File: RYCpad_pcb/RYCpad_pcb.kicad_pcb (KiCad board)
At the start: 2 copper layers, 77.2 x 117.6 mm, 66 parts, among them J1 USB_C_Receptacle_USB2.0, J2 AVR ISP, K1 KEYSW, K10 KEYSW, K11 KEYSW, K12 KEYSW, K13 KEYSW, K14 KEYSW, K15 KEYSW, K16 KEYSW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

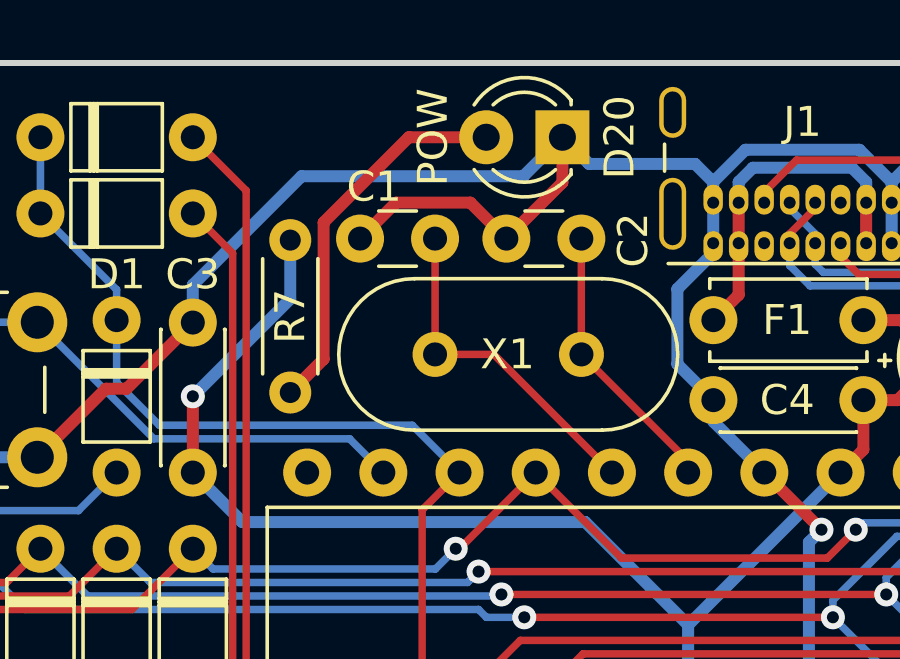
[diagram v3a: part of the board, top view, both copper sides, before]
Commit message: Make LED software-controlled
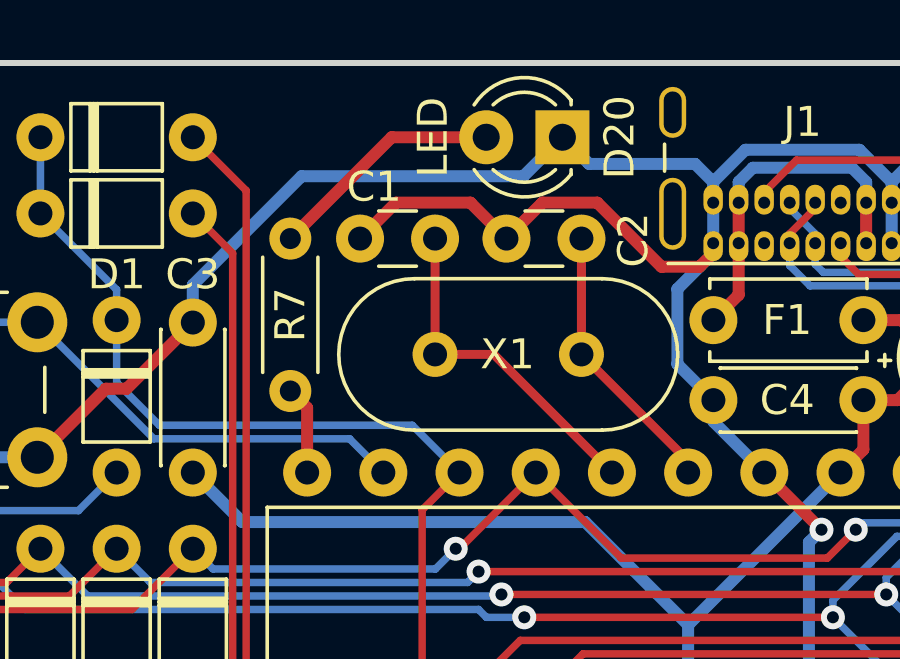
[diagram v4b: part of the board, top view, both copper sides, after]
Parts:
- C1, C2: value 22 -> 22p
- D20: value POW -> LED
- R5, R6: value 75 -> 68
- moved R7 5.13 mm to (-17.1, -54.2), turned to -90 degrees
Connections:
- J1 pad A8: Net-(J1-PadA8) -> unconnected-(J1-PadA8)
- J1 pad B8: Net-(J1-PadB8) -> unconnected-(J1-PadB8)
- J1 pad S1: Net-(J1-PadS1) -> unconnected-(J1-PadS1)
- R7 pad 2: +5V -> Net-(U1-Pad14)
- U1 pad 2: Net-(U1-Pad2) -> unconnected-(U1-Pad2)
- U1 pad 21: Net-(U1-Pad21) -> unconnected-(U1-Pad21)
- U1 pad 26: Net-(U1-Pad26) -> unconnected-(U1-Pad26)
- U1 pad 3: Net-(U1-Pad3) -> unconnected-(U1-Pad3)
- U1 pad 6: Net-(U1-Pad6) -> unconnected-(U1-Pad6)
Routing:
- net +5V: track 77.0 -> 67.9 mm, vias 1 -> 0
- net Net-(R7-Pad1): track 12.7 -> 7.93 mm
- net GND: track 140.1 -> 144.8 mm
- net Net-(U1-Pad14): track 0.00 -> 2.95 mm
